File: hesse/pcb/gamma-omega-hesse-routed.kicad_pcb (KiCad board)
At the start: 2 copper layers, 232.8 x 111.4 mm, 47 parts

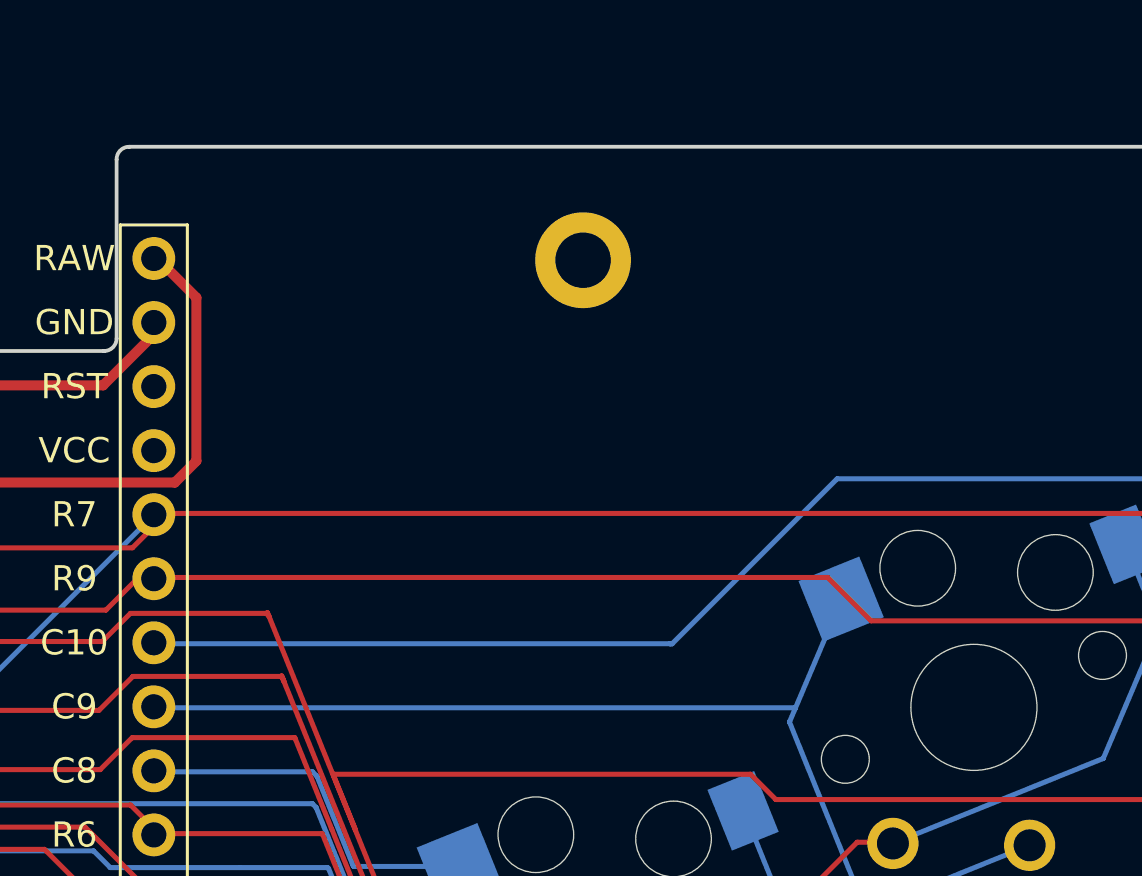
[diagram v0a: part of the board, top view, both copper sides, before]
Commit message: Refresh Hesse PCB with reset switch
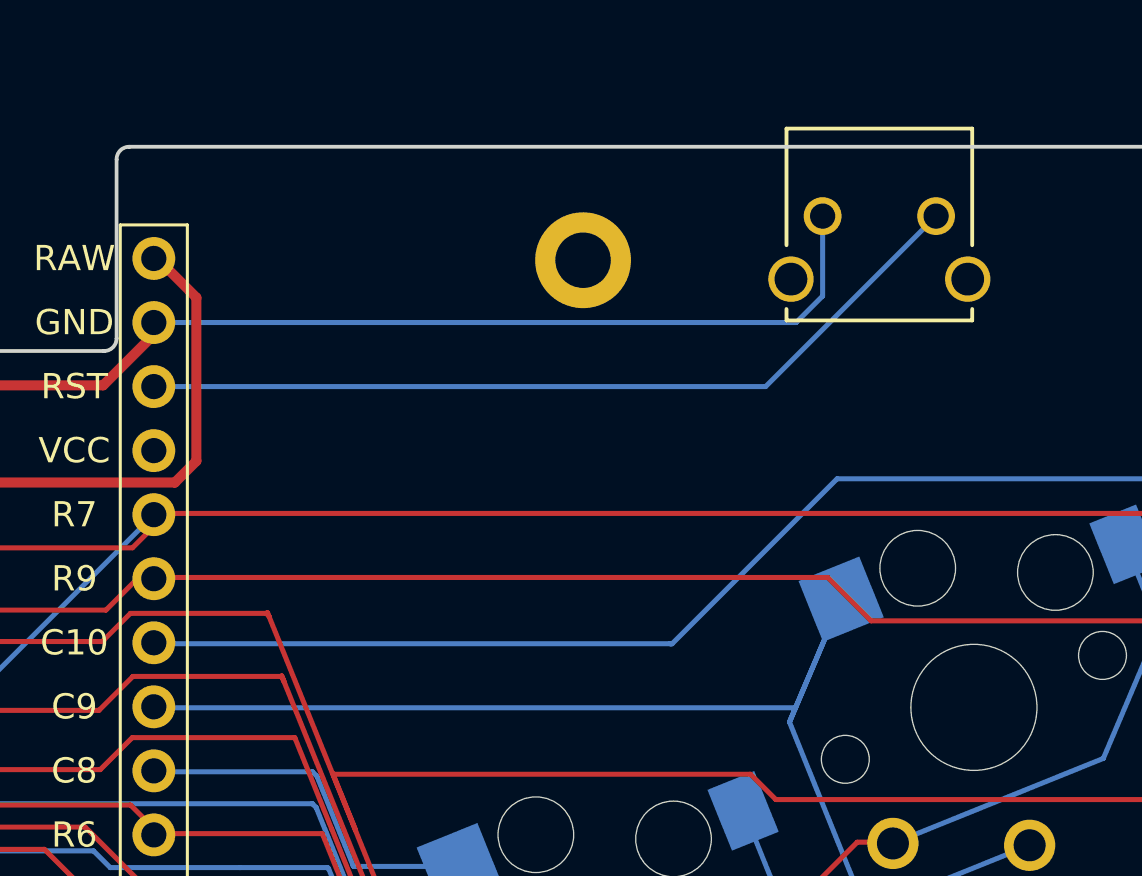
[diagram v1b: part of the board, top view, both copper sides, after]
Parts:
- added RST1: , peterjc:reset_switch_1825027-8, F.Cu at (195.3, 52.5)
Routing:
- net RST: track 0.00 -> 33.8 mm
- net GND: track 298.4 -> 328.5 mm
- net C9: track 98.0 -> 103.0 mm

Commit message: Now with ground plane
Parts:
- moved S11 0.48 mm to (110.1, 88.2)
- moved RST1 0.48 mm to (195.3, 53.0)
- moved S6 0.48 mm to (75.2, 59.0)
- moved S25 0.48 mm to (224.2, 90.5)
- moved S13 0.48 mm to (118.9, 114.6)
- moved S8 0.48 mm to (94.3, 74.3)
- moved S7 0.48 mm to (89.1, 90.5)
- moved S1 0.48 mm to (50.0, 100.5)
- moved S27 0.48 mm to (213.7, 58.2)
- moved S26 0.48 mm to (218.9, 74.3)
- moved S18 0.48 mm to (119.5, 144.7)
- moved S2 0.48 mm to (50.0, 83.5)
- moved S9 0.48 mm to (99.6, 58.2)
- moved H2 0.48 mm to (270.3, 52.7)
- moved S29 0.48 mm to (203.1, 88.2)
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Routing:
- net C8: track 87.2 -> 99.8 mm
- net C7: track 178.6 -> 167.3 mm
- net R8: track 317.1 -> 308.0 mm
- net C4: track 176.9 -> 168.4 mm
- net C1: track 205.8 -> 212.1 mm
- net C2: track 194.5 -> 200.8 mm
- net C3: track 124.2 -> 130.5 mm
- net C12: track 210.6 -> 216.8 mm
- net R6: track 362.5 -> 368.5 mm
- net C9: track 103.0 -> 108.6 mm
- net C10: track 119.0 -> 124.5 mm
- net C6: track 162.0 -> 167.5 mm
- net R9: track 258.5 -> 263.9 mm
- net C11: track 200.9 -> 205.9 mm
- net GND: track 328.5 -> 332.5 mm, vias 0 -> 1
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- added copper zone on B.Cu, net GND
- added copper zone on F.Cu, net GND
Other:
- outline, holes or cut-outs redrawn

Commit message: Polish
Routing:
- net R3: track 326.2 -> 328.4 mm
- net R7: track 331.0 -> 332.2 mm

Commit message: Route battery on right (3 vias each way, less than half the distance)
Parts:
- moved S11 0.13 mm to (110.1, 88.4)
- moved S9 0.13 mm to (99.6, 58.3)
- moved S27 0.13 mm to (213.6, 58.3)
- moved S24 0.13 mm to (238.1, 59.1)
- moved S14 0.13 mm to (125.2, 98.9)
- moved S20 0.13 mm to (263.2, 83.6)
- moved H4 0.13 mm to (270.2, 114.4)
- moved S13 0.13 mm to (118.9, 114.7)
- moved S5 0.13 mm to (72.2, 75.9)
- moved S17 0.13 mm to (104.8, 130.6)
- moved S26 0.13 mm to (218.9, 74.5)
- moved S4 0.13 mm to (69.2, 92.6)
- moved S34 0.13 mm to (226.2, 120.7)
- moved S30 0.13 mm to (196.7, 72.6)
- moved S32 0.13 mm to (188.0, 98.9)
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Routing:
- net GND: track 332.5 -> 218.7 mm, vias 1 -> 4
- net RAW: track 286.8 -> 177.7 mm, vias 0 -> 3
- net C9: track 108.6 -> 121.1 mm
- net R6: track 368.5 -> 362.4 mm
- net R7: track 332.2 -> 329.5 mm
- net C11: track 205.9 -> 208.3 mm
- net C8: track 99.8 -> 97.9 mm
- net R2: track 388.5 -> 390.3 mm
- net R5: track 495.6 -> 493.9 mm
- net C12: track 216.8 -> 217.7 mm
- net C7: track 167.3 -> 168.2 mm
- net R4: track 305.6 -> 306.4 mm
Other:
- outline, holes or cut-outs redrawn

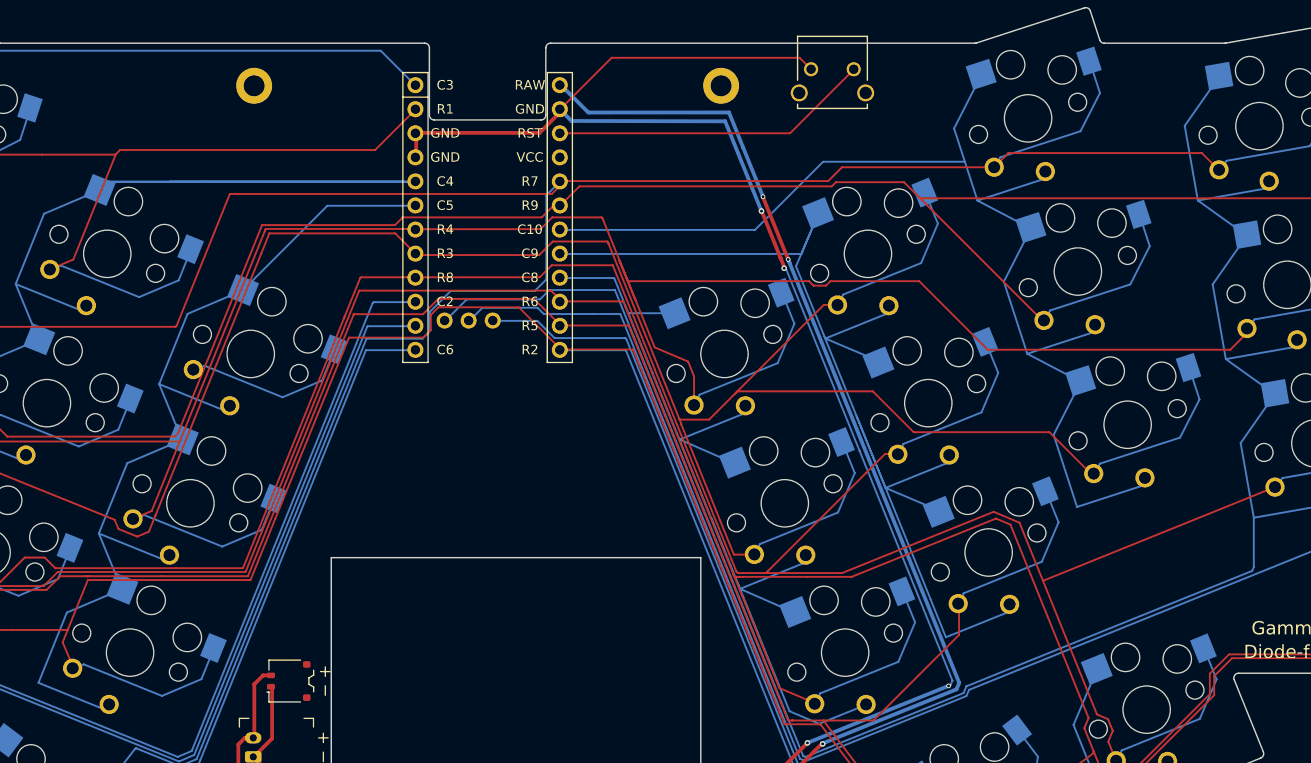
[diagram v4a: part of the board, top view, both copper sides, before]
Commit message: Avoid some vias on the battery (added one on a column)
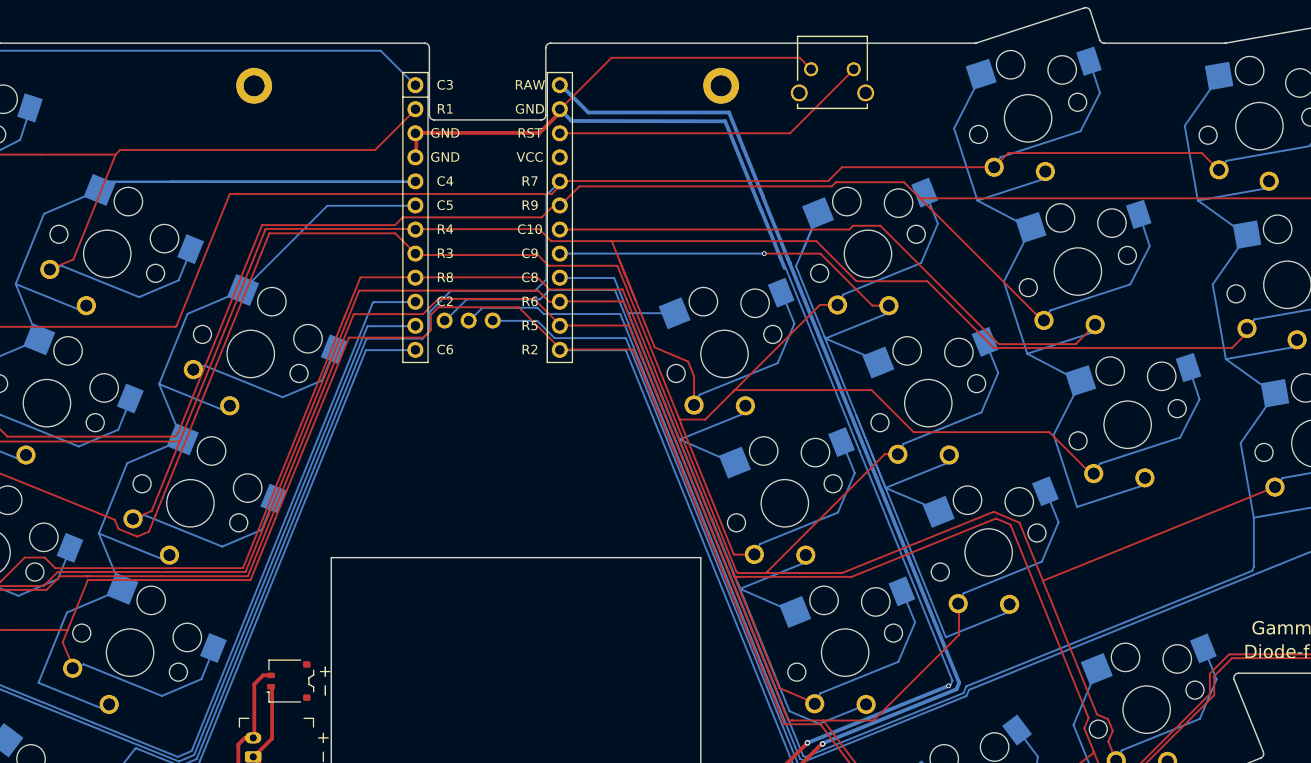
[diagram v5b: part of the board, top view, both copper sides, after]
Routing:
- net C10: track 124.5 -> 141.5 mm
- net C9: track 121.1 -> 132.6 mm, vias 0 -> 1
- net R3: track 328.4 -> 326.6 mm
- net R8: track 308.0 -> 306.3 mm
- net GND: track 218.7 -> 217.3 mm, vias 4 -> 2
- net R4: track 306.4 -> 305.3 mm
- net RAW: vias 3 -> 1

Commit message: Polish PCB
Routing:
- net C6: track 167.5 -> 157.5 mm
- net C10: track 141.5 -> 142.1 mm
